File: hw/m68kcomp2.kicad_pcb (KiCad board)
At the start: 2 copper layers, 3 parts, among them U1 mc68030rc, U2 as6c8016, U3 as6c8016

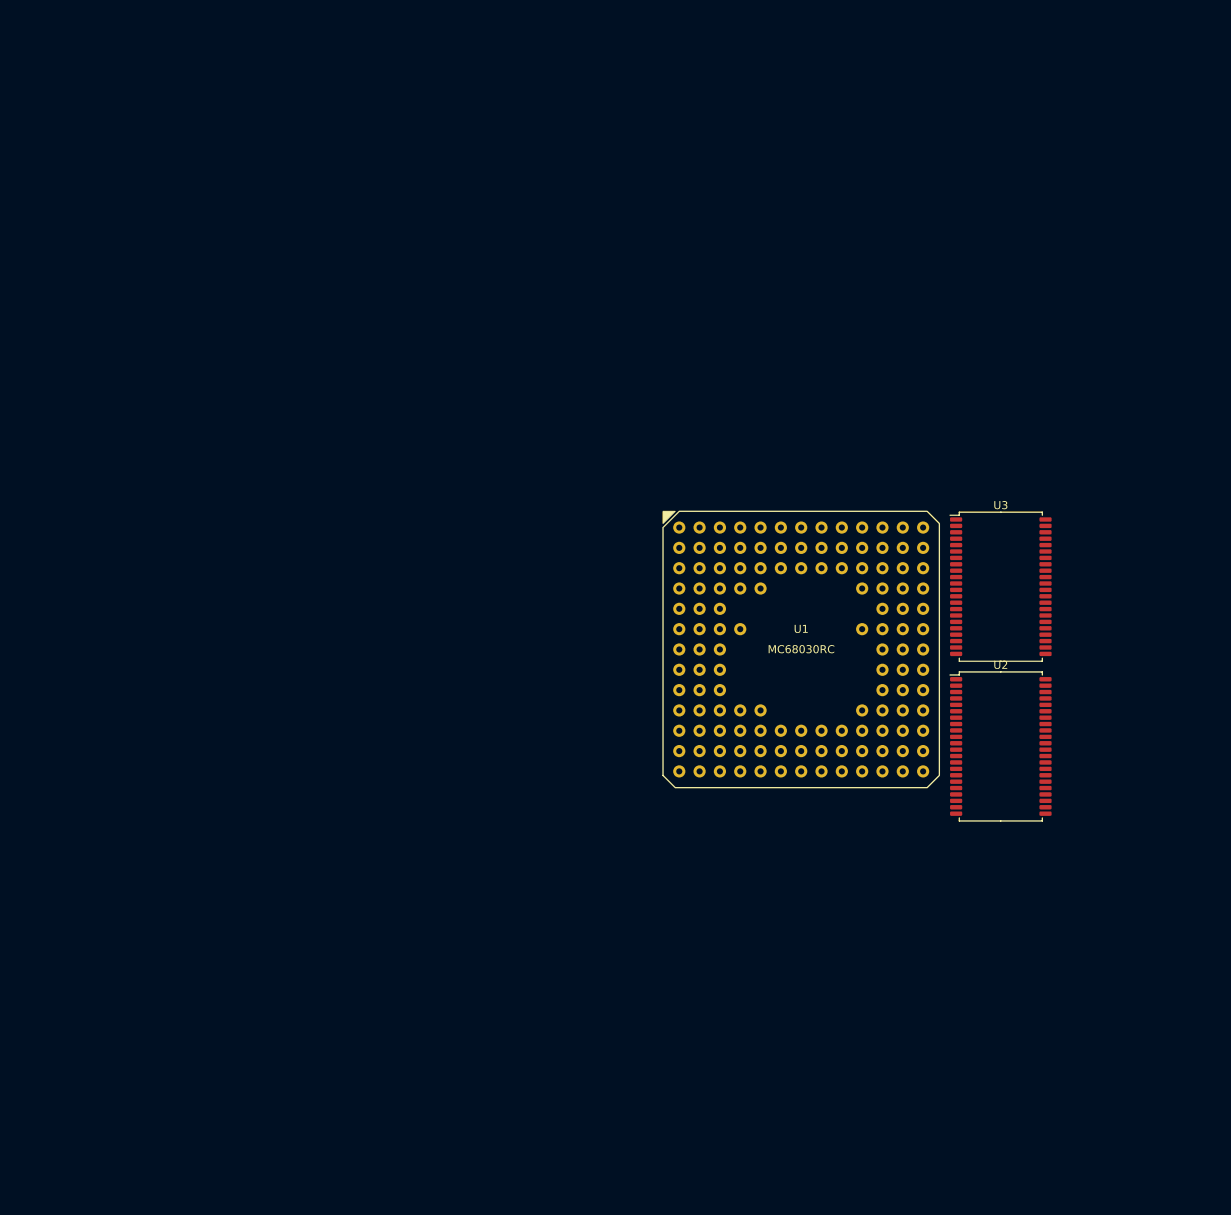
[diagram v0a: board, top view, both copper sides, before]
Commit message: BERR watchdog
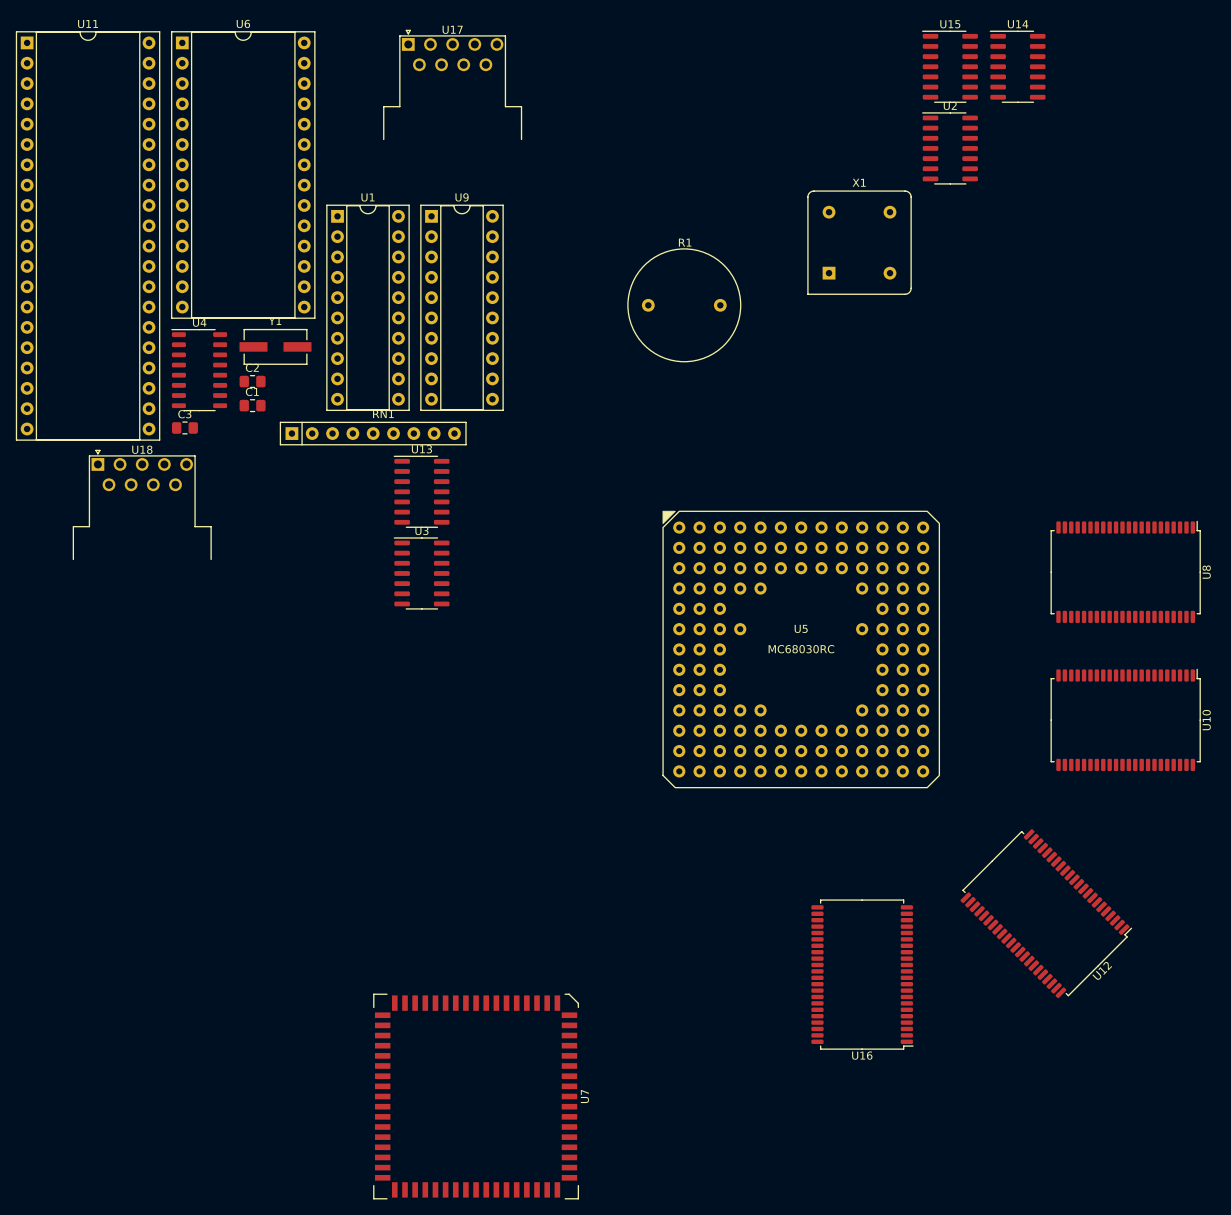
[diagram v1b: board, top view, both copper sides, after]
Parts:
- added C1: 0.1uF, Capacitor_SMD:C_0805_2012Metric_Pad1.18x1.45mm_HandSolder, F.Cu at (22.9, 43.2)
- added C2: 12pF, Capacitor_SMD:C_0805_2012Metric_Pad1.18x1.45mm_HandSolder, F.Cu at (22.9, 40.2)
- added C3: 12pF, Capacitor_SMD:C_0805_2012Metric_Pad1.18x1.45mm_HandSolder, F.Cu at (14.4, 46.0)
- added R1: 4k7, OptoDevice:R_LDR_D13.8mm_P9.0mm_Vertical, F.Cu at (72.3, 30.6)
- added RN1: 4k7, Resistor_THT:R_Array_SIP9, F.Cu at (27.8, 46.7)
- added U1: GAL16V8, Package_DIP:DIP-20_W7.62mm_Socket, F.Cu at (33.5, 19.5)
- added U10: as6c8008, Package_SO:TSOP-II-44_10.16x18.41mm_P0.8mm, F.Cu at (132.0, 82.5)
- added U11: mc68681, Package_DIP:DIP-40_W15.24mm_Socket, F.Cu at (-5.32, -2.16)
- added U12: as6c8008, Package_SO:TSOP-II-44_10.16x18.41mm_P0.8mm, F.Cu at (121.9, 106.7)
- added U13: mc1489, Package_SO:SO-14_3.9x8.65mm_P1.27mm, F.Cu at (44.0, 54.0)
- added U14: mc1488, Package_SO:SO-14_3.9x8.65mm_P1.27mm, F.Cu at (118.5, 0.82)
- added U15: mc1488, Package_SO:SO-14_3.9x8.65mm_P1.27mm, F.Cu at (110.1, 0.82)
- added U16: as6c8008, Package_SO:TSOP-II-44_10.16x18.41mm_P0.8mm, F.Cu at (99.1, 114.3)
- added U17: sera, Connector_Dsub:DSUB-9_Male_Horizontal_P2.77x2.54mm_EdgePinOffset9.40mm, F.Cu at (42.3, -1.97)
- added U18: serb, Connector_Dsub:DSUB-9_Male_Horizontal_P2.77x2.54mm_EdgePinOffset9.40mm, F.Cu at (3.53, 50.5)
- added U4: 74HC148, Package_SO:SO-16_3.9x9.9mm_P1.27mm, F.Cu at (16.2, 38.7)
- added U6: 28C256, Package_DIP:DIP-28_W15.24mm_Socket, F.Cu at (14.1, -2.16)
- added U7: mc68881, Package_LCC:PLCC-68, F.Cu at (50.8, 129.5)
- added U8: as6c8008, Package_SO:TSOP-II-44_10.16x18.41mm_P0.8mm, F.Cu at (132.0, 64.0)
- added U9: GAL16V8, Package_DIP:DIP-20_W7.62mm_Socket, F.Cu at (45.2, 19.5)
- added X1: 25.175MHz, Oscillator:Oscillator_DIP-8, F.Cu at (94.9, 26.6)
- added Y1: 3.6864MHz, Crystal:Crystal_SMD_ECS_CSM3X-2Pin_7.6x4.1mm, F.Cu at (25.7, 35.8)
- U2: value as6c8016 -> 74HC393; footprint Package_SO:TSOP-II-44_10.16x18.41mm_P0.8mm -> Package_SO:SO-14_3.9x8.65mm_P1.27mm
- U3: value as6c8016 -> 74HC10; footprint Package_SO:TSOP-II-44_10.16x18.41mm_P0.8mm -> Package_SO:SO-14_3.9x8.65mm_P1.27mm
- moved U2 75.0 mm to (110.1, 11.0)
- moved U3 72.4 mm to (44.0, 64.2)
- renumbered U1 to U5
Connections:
- U2 pad 1: /A4 -> /~{WDOG_CNT}
- U2 pad 10: /D3 -> unconnected-(U2-Pad10)
- U2 pad 11: VCC -> unconnected-(U2-Pad11)
- U2 pad 12: GND -> /WDOG_RST
- U2 pad 13: /D4 -> Net-(U2-Pad13)
- U2 pad 14: /D5 -> (no net)
- U2 pad 2: /A3 -> /WDOG_RST
- U2 pad 3: /A2 -> unconnected-(U2-Pad3)
- U2 pad 4: /A1 -> unconnected-(U2-Pad4)
- U2 pad 5: /A0 -> unconnected-(U2-Pad5)
- U2 pad 6: unconnected-(U2-Pad6) -> Net-(U2-Pad13)
- U2 pad 7: /D0 -> (no net)
- U2 pad 8: /D1 -> unconnected-(U2-Pad8)
- U2 pad 9: /D2 -> /BERR
- U3 pad 1: /A4 -> /FC2
- U3 pad 10: /D3 -> (no net)
- U3 pad 11: VCC -> (no net)
- U3 pad 12: GND -> /~{FCPU}
- U3 pad 13: /D4 -> /FC0
- U3 pad 14: /D5 -> (no net)
- U3 pad 2: /A3 -> /FC1
- U3 pad 3: /A2 -> /BERR
- U3 pad 4: /A1 -> /BERR
- U3 pad 5: /A0 -> /BERR
- U3 pad 6: unconnected-(U3-Pad6) -> /~{BERR}
- U3 pad 7: /D0 -> (no net)
- U3 pad 8: /D1 -> (no net)
- U3 pad 9: /D2 -> (no net)
- U5 pad A10: unconnected-(U1-PadA10) -> /A17
- U5 pad A11: unconnected-(U1-PadA11) -> /A15
- U5 pad A12: unconnected-(U1-PadA12) -> /A13
- U5 pad A13: unconnected-(U1-PadA13) -> /A10
- U5 pad A2: unconnected-(U1-PadA2) -> /A0
- U5 pad A3: unconnected-(U1-PadA3) -> /A30
- U5 pad A4: unconnected-(U1-PadA4) -> /A28
- U5 pad A5: unconnected-(U1-PadA5) -> /A26
- U5 pad A6: unconnected-(U1-PadA6) -> /A24
- U5 pad A7: unconnected-(U1-PadA7) -> /A23
- U5 pad A8: unconnected-(U1-PadA8) -> /A21
- U5 pad A9: unconnected-(U1-PadA9) -> /A19
- U5 pad B10: unconnected-(U1-PadB10) -> /A14
- U5 pad B11: unconnected-(U1-PadB11) -> /A12
- U5 pad B12: unconnected-(U1-PadB12) -> /A8
- U5 pad B13: unconnected-(U1-PadB13) -> /A7
- U5 pad B3: unconnected-(U1-PadB3) -> /A31
- U5 pad B4: unconnected-(U1-PadB4) -> /A29
- U5 pad B5: unconnected-(U1-PadB5) -> /A27
- U5 pad B6: unconnected-(U1-PadB6) -> /A25
- U5 pad B7: unconnected-(U1-PadB7) -> /A22
- U5 pad B8: unconnected-(U1-PadB8) -> /A20
- U5 pad B9: unconnected-(U1-PadB9) -> /A16
- U5 pad C1: unconnected-(U1-PadC1) -> /FC1
- U5 pad C10: unconnected-(U1-PadC10) -> /A11
- U5 pad C11: unconnected-(U1-PadC11) -> /A9
- U5 pad C12: unconnected-(U1-PadC12) -> /A5
- U5 pad C13: unconnected-(U1-PadC13) -> /A4
- U5 pad C4: unconnected-(U1-PadC4) -> /A1
- U5 pad C8: unconnected-(U1-PadC8) -> /A18
- U5 pad D1: unconnected-(U1-PadD1) -> /FC2
- U5 pad D11: unconnected-(U1-PadD11) -> /A6
- U5 pad D12: unconnected-(U1-PadD12) -> /A3
- U5 pad D13: unconnected-(U1-PadD13) -> /A2
- U5 pad D2: unconnected-(U1-PadD2) -> /FC0
- U5 pad E1: unconnected-(U1-PadE1) -> /CLK
- U5 pad E2: unconnected-(U1-PadE2) -> /~{AVEC}
- U5 pad G12: unconnected-(U1-PadG12) -> Net-(U4-Pad6)
- U5 pad G13: unconnected-(U1-PadG13) -> Net-(U4-Pad7)
- U5 pad H1: unconnected-(U1-PadH1) -> /~{BERR}
- U5 pad H13: unconnected-(U1-PadH13) -> Net-(U4-Pad9)
- U5 pad K11: unconnected-(U1-PadK11) -> /D5
- U5 pad K12: unconnected-(U1-PadK12) -> /D1
- U5 pad K13: unconnected-(U1-PadK13) -> /D0
- U5 pad L10: unconnected-(U1-PadL10) -> /D10
- U5 pad L11: unconnected-(U1-PadL11) -> /D7
- U5 pad L12: unconnected-(U1-PadL12) -> /D4
- U5 pad L13: unconnected-(U1-PadL13) -> /D2
- U5 pad L4: unconnected-(U1-PadL4) -> /D30
- U5 pad M10: unconnected-(U1-PadM10) -> /D12
- U5 pad M11: unconnected-(U1-PadM11) -> /D9
- U5 pad M12: unconnected-(U1-PadM12) -> /D6
- U5 pad M13: unconnected-(U1-PadM13) -> /D3
- U5 pad M3: unconnected-(U1-PadM3) -> /D29
- U5 pad M4: unconnected-(U1-PadM4) -> /D27
- U5 pad M5: unconnected-(U1-PadM5) -> /D24
- U5 pad M6: unconnected-(U1-PadM6) -> /D22
- U5 pad M7: unconnected-(U1-PadM7) -> /D20
- U5 pad M8: unconnected-(U1-PadM8) -> /D17
- U5 pad M9: unconnected-(U1-PadM9) -> /D14
- U5 pad N1: unconnected-(U1-PadN1) -> /D31
- U5 pad N10: unconnected-(U1-PadN10) -> /D15
- U5 pad N11: unconnected-(U1-PadN11) -> /D13
- U5 pad N12: unconnected-(U1-PadN12) -> /D11
- U5 pad N13: unconnected-(U1-PadN13) -> /D8
- U5 pad N2: unconnected-(U1-PadN2) -> /D28
- U5 pad N3: unconnected-(U1-PadN3) -> /D26
- U5 pad N4: unconnected-(U1-PadN4) -> /D25
- U5 pad N5: unconnected-(U1-PadN5) -> /D23
- U5 pad N6: unconnected-(U1-PadN6) -> /D21
- U5 pad N7: unconnected-(U1-PadN7) -> /D19
- U5 pad N8: unconnected-(U1-PadN8) -> /D18
- U5 pad N9: unconnected-(U1-PadN9) -> /D16

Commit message: fixed resistor footprint assignments, changed PCB to 4-layer
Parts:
- added BT1: 3V, Battery:BatteryHolder_Keystone_1060_1x2032, F.Cu at (251.5, 63.5)
- added C10: 10uF, Capacitor_SMD:C_0805_2012Metric_Pad1.18x1.45mm_HandSolder, F.Cu at (51.6, -22.9)
- added C11: 0.1u, Capacitor_SMD:C_0805_2012Metric_Pad1.18x1.45mm_HandSolder, F.Cu at (56.5, -18.2)
- added C12: 0.1uF, Capacitor_SMD:C_0805_2012Metric_Pad1.18x1.45mm_HandSolder, F.Cu at (71.1, -25.9)
- added C13: 0.1u, Capacitor_SMD:C_0805_2012Metric_Pad1.18x1.45mm_HandSolder, F.Cu at (61.5, -27.2)
- added C14: 330pF, Capacitor_SMD:C_0805_2012Metric_Pad1.18x1.45mm_HandSolder, F.Cu at (66.3, -22.9)
- added C15: 0.1u, Capacitor_SMD:C_0805_2012Metric_Pad1.18x1.45mm_HandSolder, F.Cu at (46.8, -18.8)
- added C16: 10uF, Capacitor_SMD:C_0805_2012Metric_Pad1.18x1.45mm_HandSolder, F.Cu at (42.0, -15.2)
- added C17: 0.1u, Capacitor_SMD:C_0805_2012Metric_Pad1.18x1.45mm_HandSolder, F.Cu at (66.1, -16.8)
- added C18: 0.1uF, Capacitor_SMD:C_0805_2012Metric_Pad1.18x1.45mm_HandSolder, F.Cu at (66.3, -25.9)
- added C19: 0.1u, Capacitor_SMD:C_0805_2012Metric_Pad1.18x1.45mm_HandSolder, F.Cu at (56.7, -24.2)
- added C20: 0.1u, Capacitor_SMD:C_0805_2012Metric_Pad1.18x1.45mm_HandSolder, F.Cu at (56.7, -27.2)
- added C21: 330pF, Capacitor_SMD:C_0805_2012Metric_Pad1.18x1.45mm_HandSolder, F.Cu at (76.7, -33.1)
- added C22: 0.1u, Capacitor_SMD:C_0805_2012Metric_Pad1.18x1.45mm_HandSolder, F.Cu at (46.8, -24.8)
- added C23: 0.1u, Capacitor_SMD:C_0805_2012Metric_Pad1.18x1.45mm_HandSolder, F.Cu at (66.1, -19.9)
- added C24: 0.1u, Capacitor_SMD:C_0805_2012Metric_Pad1.18x1.45mm_HandSolder, F.Cu at (56.5, -21.2)
- added C25: 0.1u, Capacitor_SMD:C_0805_2012Metric_Pad1.18x1.45mm_HandSolder, F.Cu at (61.3, -18.2)
- added C26: 0.1u, Capacitor_SMD:C_0805_2012Metric_Pad1.18x1.45mm_HandSolder, F.Cu at (51.6, -16.8)
- added C27: 0.1u, Capacitor_SMD:C_0805_2012Metric_Pad1.18x1.45mm_HandSolder, F.Cu at (51.6, -19.9)
- added C28: 0.1u, Capacitor_SMD:C_0805_2012Metric_Pad1.18x1.45mm_HandSolder, F.Cu at (71.1, -22.9)
- added C29: 0.1u, Capacitor_SMD:C_0805_2012Metric_Pad1.18x1.45mm_HandSolder, F.Cu at (61.3, -21.2)
- added C30: 0.1u, Capacitor_SMD:C_0805_2012Metric_Pad1.18x1.45mm_HandSolder, F.Cu at (46.8, -21.8)
- added C31: 0.1u, Capacitor_SMD:C_0805_2012Metric_Pad1.18x1.45mm_HandSolder, F.Cu at (81.5, -33.1)
- added C32: 0.1u, Capacitor_SMD:C_0805_2012Metric_Pad1.18x1.45mm_HandSolder, F.Cu at (42.0, -19.9)
- added C33: 0.1u, Capacitor_SMD:C_0805_2012Metric_Pad1.18x1.45mm_HandSolder, F.Cu at (61.5, -24.2)
- added C34: 0.1u, Capacitor_SMD:C_0805_2012Metric_Pad1.18x1.45mm_HandSolder, F.Cu at (46.8, -15.8)
- added C35: 0.1u, Capacitor_SMD:C_0805_2012Metric_Pad1.18x1.45mm_HandSolder, F.Cu at (51.9, -25.9)
- added C36: 0.1u, Capacitor_SMD:C_0805_2012Metric_Pad1.18x1.45mm_HandSolder, F.Cu at (76.7, -30.1)
- added C4: 12pF, Capacitor_SMD:C_0805_2012Metric_Pad1.18x1.45mm_HandSolder, F.Cu at (-103.2, 1.02)
- added C5: 12pF, Capacitor_SMD:C_0805_2012Metric_Pad1.18x1.45mm_HandSolder, F.Cu at (-108.0, 1.02)
- added C6: 12pF, Capacitor_SMD:C_0805_2012Metric_Pad1.18x1.45mm_HandSolder, F.Cu at (-124.8, 27.9)
- added C7: 12pF, Capacitor_SMD:C_0805_2012Metric_Pad1.18x1.45mm_HandSolder, F.Cu at (-112.8, 1.02)
- added C8: 10uF, Capacitor_SMD:CP_Elec_4x4.5, F.Cu at (61.1, -31.6)
- added C9: 22uF, Capacitor_SMD:CP_Elec_4x4.5, F.Cu at (53.4, -31.6)
- added D1: 1N4148, Diode_THT:D_DO-35_SOD27_P7.62mm_Horizontal, F.Cu at (-78.2, 73.4)
- added D2: 1N4148, Diode_THT:D_DO-35_SOD27_P7.62mm_Horizontal, F.Cu at (-57.0, 63.9)
- added D3: 1N4148, Diode_THT:D_DO-35_SOD27_P7.62mm_Horizontal, F.Cu at (-67.5, 74.5)
- added D4: 1N4148, Diode_THT:D_DO-35_SOD27_P7.62mm_Horizontal, F.Cu at (-67.5, 71.0)
- added D5: 1N4148, Diode_THT:D_DO-35_SOD27_P7.62mm_Horizontal, F.Cu at (-78.2, 69.8)
- added D6: 1N4148, Diode_THT:D_DO-35_SOD27_P7.62mm_Horizontal, F.Cu at (-57.0, 67.4)
- added D7: 1N4148, Diode_THT:D_DO-35_SOD27_P7.62mm_Horizontal, F.Cu at (-113.7, -2.26)
- added D8: 1N4148, Diode_THT:D_DO-35_SOD27_P7.62mm_Horizontal, F.Cu at (-102.9, -2.26)
- added D9: ACTLED, LED_SMD:LED_0805_2012Metric_Pad1.15x1.40mm_HandSolder, F.Cu at (-98.4, 1.03)
- added J1: SWRST, Connector_PinHeader_2.54mm:PinHeader_1x02_P2.54mm_Vertical, F.Cu at (-29.1, 46.0)
- added J2: CFMASTER, Connector_PinHeader_2.54mm:PinHeader_1x02_P2.54mm_Vertical, F.Cu at (-40.1, 10.1)
- added J3: AVR-ISP, Connector_IDC:IDC-Header_2x03_P2.54mm_Vertical, F.Cu at (231.1, 106.7)
- added J4: ACTLED, Connector_PinHeader_2.54mm:PinHeader_1x02_P2.54mm_Vertical, F.Cu at (-38.1, -20.3)
- added J5: ATX-24, Connector_Molex:Molex_Mini-Fit_Jr_5566-24A_2x12_P4.20mm_Vertical, F.Cu at (287.0, 121.9)
- added J6: VREG_3V3, Connector_PinHeader_2.54mm:PinHeader_1x02_P2.54mm_Vertical, F.Cu at (72.0, -32.2)
- added JP1: I/O nocache, Jumper:SolderJumper-2_P1.3mm_Bridged_RoundedPad1.0x1.5mm, F.Cu at (-44.6, 63.8)
- added R2: 10k, Resistor_SMD:R_0805_2012Metric_Pad1.20x1.40mm_HandSolder, F.Cu at (-39.6, 60.5)
- added R3: 4k7, Resistor_SMD:R_0805_2012Metric_Pad1.20x1.40mm_HandSolder, F.Cu at (-93.4, 43.2)
- added R4: 4k7, Resistor_SMD:R_0805_2012Metric_Pad1.20x1.40mm_HandSolder, F.Cu at (-113.7, 53.3)
- added R5: 4k7, Resistor_SMD:R_0805_2012Metric_Pad1.20x1.40mm_HandSolder, F.Cu at (-64.7, -3.90)
- added R6: 1k, Resistor_SMD:R_0805_2012Metric_Pad1.20x1.40mm_HandSolder, F.Cu at (-72.2, 23.2)
- added R7: 1k, Resistor_SMD:R_0805_2012Metric_Pad1.20x1.40mm_HandSolder, F.Cu at (-39.3, 0.13)
- added RN2: 4k7, Resistor_THT:R_Array_SIP9, F.Cu at (-44.5, 37.2)
- added SW1: SWRST, Button_Switch_SMD:SW_SPST_EVPBF, F.Cu at (-16.9, 38.8)
- added SW2: SWPWR, Connector_PinHeader_2.54mm:PinHeader_1x02_P2.54mm_Vertical, F.Cu at (67.3, -32.2)
- added TP1: TPCLK, TestPoint:TestPoint_Pad_D1.5mm, F.Cu at (-69.6, 88.3)
- added TP10: TP3V3, TestPoint:TestPoint_Pad_D1.5mm, F.Cu at (41.4, -8.96)
- added TP11: TPN12V, TestPoint:TestPoint_Pad_D1.5mm, F.Cu at (95.0, -45.9)
- added TP12: TP5V, TestPoint:TestPoint_Pad_D1.5mm, F.Cu at (46.2, -12.5)
- added TP2: TPRST, TestPoint:TestPoint_Pad_D1.5mm, F.Cu at (-93.5, 83.9)
- added TP3: TPRW, TestPoint:TestPoint_Pad_D1.5mm, F.Cu at (-56.5, 77.4)
- added TP4: TPAS, TestPoint:TestPoint_Pad_D1.5mm, F.Cu at (-61.1, 81.6)
- added TP5: TPSZ0, TestPoint:TestPoint_Pad_D1.5mm, F.Cu at (-46.0, 67.3)
- added TP6: TPSZ1, TestPoint:TestPoint_Pad_D1.5mm, F.Cu at (-61.1, 78.1)
- added TP7: TPDS0, TestPoint:TestPoint_Pad_D1.5mm, F.Cu at (-78.0, 98.5)
- added TP8: TPDS1, TestPoint:TestPoint_Pad_D1.5mm, F.Cu at (-25.0, 45.5)
- added TP9: TP12V, TestPoint:TestPoint_Pad_D1.5mm, F.Cu at (51.0, -13.6)
- added U19: 74LVC125, Package_SO:SO-14_3.9x8.65mm_P1.27mm, F.Cu at (256.5, 132.1)
- added U20: mc1489, Package_SO:SO-14_3.9x8.65mm_P1.27mm, F.Cu at (200.7, 55.9)
- added U21: mc1488, Package_SO:SO-14_3.9x8.65mm_P1.27mm, F.Cu at (180.3, 58.4)
- added U22: mc1488, Package_SO:SO-14_3.9x8.65mm_P1.27mm, F.Cu at (165.1, 55.9)
- added U23: sdcard, Connector_Card:SD_TE_2041021, F.Cu at (246.4, 167.6)
- added U24: sera, Connector_Dsub:DSUB-9_Male_Horizontal_P2.77x2.84mm_EdgePinOffset7.70mm_Housed_MountingHolesOffset9.12mm, F.Cu at (170.2, 40.6)
- added U25: serb, Connector_Dsub:DSUB-9_Male_Horizontal_P2.77x2.84mm_EdgePinOffset7.70mm_Housed_MountingHolesOffset9.12mm, F.Cu at (205.7, 40.6)
- added U26: 28C256, Package_DIP:DIP-28_W15.24mm_Socket, F.Cu at (144.8, 148.6)
- added U27: as6c8008, Package_SO:TSOP-II-44_10.16x18.41mm_P0.8mm, F.Cu at (205.2, 180.4)
- added U28: as6c8008, Package_SO:TSOP-II-44_10.16x18.41mm_P0.8mm, F.Cu at (205.7, 151.7)
- added U29: as6c8008, Package_SO:TSOP-II-44_10.16x18.41mm_P0.8mm, F.Cu at (181.3, 180.3)
- added U30: as6c8008, Package_SO:TSOP-II-44_10.16x18.41mm_P0.8mm, F.Cu at (181.3, 151.7)
- added U31: exp_conn, m68kcomp2:pcix8slot, F.Cu at (61.0, 70.3)
- added U32: exp_conn, m68kcomp2:pcix8slot, F.Cu at (87.1, 71.3)
- added U33: LM1117-3.3, Package_TO_SOT_SMD:SOT-223-3_TabPin2, F.Cu at (274.3, 142.2)
- added Y2: 32.768kHz, Crystal:Crystal_SMD_ECS_CSM3X-2Pin_7.6x4.1mm, F.Cu at (-54.8, 16.7)
- C1: value 0.1uF -> 10uF
- C2: value 12pF -> 10uF
- C3: value 12pF -> 0.1uF
- R1: value 4k7 -> 10k; footprint OptoDevice:R_LDR_D13.8mm_P9.0mm_Vertical -> Resistor_SMD:R_0805_2012Metric_Pad1.20x1.40mm_HandSolder
- U1: value GAL16V8 -> GAL20V8; footprint Package_DIP:DIP-20_W7.62mm_Socket -> Package_DIP:DIP-24_W7.62mm_Socket
- U10: value as6c8008 -> mc68881; footprint Package_SO:TSOP-II-44_10.16x18.41mm_P0.8mm -> Package_LCC:PLCC-68_THT-Socket
- U11: value mc68681 -> 74HC393; footprint Package_DIP:DIP-40_W15.24mm_Socket -> Package_SO:SO-14_3.9x8.65mm_P1.27mm
- U12: value as6c8008 -> ATmega328PB-A; footprint Package_SO:TSOP-II-44_10.16x18.41mm_P0.8mm -> Package_QFP:TQFP-32_7x7mm_P0.8mm
- U13: value mc1489 -> cfconn; footprint Package_SO:SO-14_3.9x8.65mm_P1.27mm -> Connector_Card:CF-Card_3M_N7E50-7516PK-20-WF
- U14: value mc1488 -> ATA0; footprint Package_SO:SO-14_3.9x8.65mm_P1.27mm -> Connector_IDC:IDC-Header_2x20_P2.54mm_Vertical
- U15: value mc1488 -> mouse; footprint Package_SO:SO-14_3.9x8.65mm_P1.27mm -> m68kcomp2:minidin6
- U16: value as6c8008 -> kbd; footprint Package_SO:TSOP-II-44_10.16x18.41mm_P0.8mm -> m68kcomp2:minidin6
- U17: value sera -> ds1501; footprint Connector_Dsub:DSUB-9_Male_Horizontal_P2.77x2.54mm_EdgePinOffset9.40mm -> Package_SO:SOIC-28W_7.5x17.9mm_P1.27mm
- U18: value serb -> mc68681; footprint Connector_Dsub:DSUB-9_Male_Horizontal_P2.77x2.54mm_EdgePinOffset9.40mm -> Package_DIP:DIP-40_W15.24mm_Socket
- U2: value 74HC393 -> GAL16V8; footprint Package_SO:SO-14_3.9x8.65mm_P1.27mm -> Package_DIP:DIP-20_W7.62mm_Socket
- U3: value 74HC10 -> NE555D; footprint Package_SO:SO-14_3.9x8.65mm_P1.27mm -> Package_SO:SOIC-8_3.9x4.9mm_P1.27mm
- U4: value 74HC148 -> 74HC10; footprint Package_SO:SO-16_3.9x9.9mm_P1.27mm -> Package_SO:SO-14_3.9x8.65mm_P1.27mm
- U5: value mc68030rc -> 74LS14; footprint m68kcomp2:mc68030rc -> Package_SO:SO-14_3.9x8.65mm_P1.27mm
- U6: value 28C256 -> 74HC148; footprint Package_DIP:DIP-28_W15.24mm_Socket -> Package_SO:SO-16_3.9x9.9mm_P1.27mm
- U7: value mc68881 -> 74HC138; footprint Package_LCC:PLCC-68 -> Package_SO:SO-16_3.9x9.9mm_P1.27mm
- U8: value as6c8008 -> mc68030rc; footprint Package_SO:TSOP-II-44_10.16x18.41mm_P0.8mm -> m68kcomp2:mc68030rc
- moved U17 229.0 mm to (251.5, 91.4)
- moved X1 218.7 mm to (-112.2, 96.9)
- moved U16 179.9 mm to (254.0, 22.9)
- moved U9 178.5 mm to (-125.2, 72.8)
- moved U14 170.1 mm to (22.1, 141.0)
- moved U2 168.6 mm to (-56.5, 37.1)
- moved U5 167.2 mm to (-75.6, 81.4)
- moved U1 133.0 mm to (-89.5, 70.2)
- moved U6 132.2 mm to (-95.9, 71.1)
- moved C2 130.8 mm to (-94.0, 99.0)
- moved C1 127.2 mm to (-97.7, 83.6)
- moved U15 125.5 mm to (233.7, 22.9), turned to 180 degrees
- moved C3 125.0 mm to (-98.8, 99.0)
- moved R1 120.5 mm to (-44.4, 60.5)
- moved U18 113.6 mm to (114.3, 25.4)
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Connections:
- C1 pad 1: VCC -> Net-(C1-Pad1)
- C3 pad 1: unconnected-(C3-Pad1) -> VCC
- C3 pad 2: unconnected-(C3-Pad2) -> GND
- R1 pad 2: /~{FPU} -> Net-(C1-Pad1)
- RN1 pad 2: /~{IRQ0} -> ~{IRQ0}
- RN1 pad 3: /~{IRQ1} -> ~{IRQ1}
- RN1 pad 4: /~{IRQ2} -> ~{IRQ2}
- RN1 pad 5: /~{IRQ3} -> ~{IRQ3}
- RN1 pad 6: /~{IRQ4} -> ~{IRQ4}
- RN1 pad 7: /~{IRQ5} -> ~{IRQ5}
- U1 pad 1: /CLK -> A13
- U1 pad 10: GND -> A22
- U1 pad 11: unconnected-(U1-Pad11) -> A23
- U1 pad 12: unconnected-(U1-Pad12) -> GND
- U1 pad 13: unconnected-(U1-Pad13) -> A24
- U1 pad 14: /WDOG_RST -> A25
- U1 pad 15: /~{WDOG_CNT} -> unconnected-(U1-Pad15)
- U1 pad 17: unconnected-(U1-Pad17) -> ~{DUARTEN}
- U1 pad 18: unconnected-(U1-Pad18) -> ~{RTCEN}
- U1 pad 19: unconnected-(U1-Pad19) -> ~{AUXEN}
- U1 pad 2: /~{AS} -> A14
- U1 pad 20: VCC -> ~{ATA1EN}
- U1 pad 3: /~{DSACK0} -> A15
- U1 pad 4: /~{DSACK1} -> A16
- U1 pad 5: /~{AVEC} -> A17
- U1 pad 6: unconnected-(U1-Pad6) -> A18
- U1 pad 7: unconnected-(U1-Pad7) -> A19
- U1 pad 8: unconnected-(U1-Pad8) -> A20
- U1 pad 9: unconnected-(U1-Pad9) -> A21
- U10 pad 1: /A4 -> D2
- U10 pad 10: /D9 -> VCC
- U10 pad 11: VCC -> /FPUCLK
- U10 pad 13: /D10 -> ~{RESET}
- U10 pad 14: /D11 -> GND
- U10 pad 16: unconnected-(U10-Pad16) -> VCC
- U10 pad 17: unconnected-(U10-Pad17) -> VCC
- U10 pad 18: /A19 -> VCC
- U10 pad 19: /A18 -> GND
- U10 pad 2: /A3 -> D1
- U10 pad 20: /A17 -> /~{DS}
- U10 pad 21: /A16 -> ~{AS}
- U10 pad 22: /A15 -> A4
- U10 pad 23: /A14 -> A3
- U10 pad 24: /A13 -> A2
- U10 pad 25: /A12 -> A1
- U10 pad 26: /A11 -> VCC
- U10 pad 27: /A10 -> VCC
- U10 pad 28: /A9 -> R/~{W}
- U10 pad 29: unconnected-(U10-Pad29) -> /~{FPUEN}
- U10 pad 3: /A2 -> D0
- U10 pad 30: unconnected-(U10-Pad30) -> GND
- U10 pad 31: /D12 -> ~{DSACK0}
- U10 pad 32: /D13 -> ~{DSACK1}
- U10 pad 33: VCC -> D31
- U10 pad 34: GND -> D30
- U10 pad 35: /D14 -> D29
- U10 pad 36: /D15 -> D28
- U10 pad 37: unconnected-(U10-Pad37) -> D27
- U10 pad 38: unconnected-(U10-Pad38) -> D26
- U10 pad 39: /A8 -> D25
- U10 pad 4: /A1 -> /~{FPU}
- U10 pad 40: unconnected-(U10-Pad40) -> D24
- U10 pad 41: unconnected-(U10-Pad41) -> GND
- U10 pad 42: /A7 -> D23
- U10 pad 43: /A6 -> VCC
- U10 pad 44: /A5 -> D22
- U10 pad 5: /A0 -> GND
- U10 pad 6: unconnected-(U10-Pad6) -> GND
- U10 pad 7: unconnected-(U10-Pad7) -> GND
- U10 pad 8: unconnected-(U10-Pad8) -> GND
- U10 pad 9: /D8 -> GND
- U11 pad 1: /A2 -> /~{WDOG_CNT}
- U11 pad 10: /RXDB -> unconnected-(U11-Pad10)
- U11 pad 11: /TXDB -> unconnected-(U11-Pad11)
- U11 pad 12: /RTRB -> /WDOG_RST
- U11 pad 13: unconnected-(U11-Pad13) -> Net-(U11-Pad13)
- U11 pad 14: /DTRB -> (no net)
- U11 pad 2: GND -> /WDOG_RST
- U11 pad 3: /A3 -> unconnected-(U11-Pad3)
- U11 pad 4: /CTSB -> unconnected-(U11-Pad4)
- U11 pad 5: /A4 -> unconnected-(U11-Pad5)
- U11 pad 6: /A5 -> Net-(U11-Pad13)
- U11 pad 7: /CTSA -> (no net)
- U11 pad 8: unconnected-(U11-Pad8) -> Net-(U11-Pad8)
- U12 pad 1: /A4 -> /io/MCLK
- U12 pad 10: /D17 -> D30
- U12 pad 11: VCC -> D31
- U12 pad 12: GND -> ~{IRQ2}
- U12 pad 13: /D18 -> /io/~{SDBUFEN}
- U12 pad 14: /D19 -> /io/~{SD_CS}
- U12 pad 15: unconnected-(U12-Pad15) -> /io/MOSI
- U12 pad 16: unconnected-(U12-Pad16) -> /io/MISO
- U12 pad 17: unconnected-(U12-Pad17) -> /io/SCK
- U12 pad 18: /A19 -> VCC
- U12 pad 19: /A18 -> A4
- U12 pad 2: /A3 -> D28
- U12 pad 20: /A17 -> unconnected-(U12-Pad20)
- U12 pad 21: /A16 -> GND
- U12 pad 22: /A15 -> A5
- U12 pad 23: /A14 -> D24
- U12 pad 24: /A13 -> D25
- U12 pad 25: /A12 -> D26
- U12 pad 26: /A11 -> D27
- U12 pad 27: /A10 -> R/~{W}
- U12 pad 28: /A9 -> ~{AUXEN}
- U12 pad 29: unconnected-(U12-Pad29) -> ~{RESET}
- U12 pad 3: /A2 -> A2
- U12 pad 30: unconnected-(U12-Pad30) -> /io/KBDATA
- U12 pad 31: /D20 -> /io/MDATA
- U12 pad 32: /D21 -> /io/KBCLK
- U12 pad 4: /A1 -> VCC
- U12 pad 5: /A0 -> GND
- U12 pad 6: unconnected-(U12-Pad6) -> A3
- U12 pad 7: unconnected-(U12-Pad7) -> ~{DSACK0}
- U12 pad 8: unconnected-(U12-Pad8) -> ~{IACK2}
- U12 pad 9: /D16 -> D29
- U13 pad 1: /RXDA_232 -> GND
- U13 pad 10: /RXDB_232 -> GND
- U13 pad 11: /CTSB -> GND
- U13 pad 12: unconnected-(U13-Pad12) -> GND
- U13 pad 13: /CTSB_232 -> VCC
- U13 pad 14: VCC -> GND
- U13 pad 2: unconnected-(U13-Pad2) -> D27
- U13 pad 3: /RXDA -> D28
- U13 pad 4: /CTSA_232 -> D29
- U13 pad 5: unconnected-(U13-Pad5) -> D30
- U13 pad 6: /CTSA -> D31
- U13 pad 7: GND -> ~{ATA0EN}
- U13 pad 8: /RXDB -> GND
- U13 pad 9: unconnected-(U13-Pad9) -> GND
- U14 pad 1: -12V -> ~{RESET}
- U14 pad 10: unconnected-(U14-Pad10) -> D19
- U14 pad 11: /RTRB_232 -> D27
- U14 pad 12: /RTRB -> D20
- U14 pad 13: unconnected-(U14-Pad13) -> D26
- U14 pad 14: +12V -> D21
- U14 pad 2: /TXDA -> GND
- U14 pad 3: /TXDA_232 -> D31
- U14 pad 4: /RTRA -> D16
- U14 pad 5: /RTRA -> D30
- U14 pad 6: /RTRA_232 -> D17
- U14 pad 7: GND -> D29
- U14 pad 8: /TXDB_232 -> D18
- U14 pad 9: /TXDB -> D28
- U15 pad 1: -12V -> /io/MDATA
- U15 pad 2: /DTRA -> unconnected-(U15-Pad2)
- U15 pad 3: /DTRA_232 -> GND
- U15 pad 4: /DTRB -> VCC
- U15 pad 5: /DTRB -> /io/MCLK
- U15 pad 6: /DTRB_232 -> unconnected-(U15-Pad6)
- U16 pad 1: /A4 -> /io/KBDATA
- U16 pad 2: /A3 -> unconnected-(U16-Pad2)
- U16 pad 3: /A2 -> GND
- U16 pad 4: /A1 -> VCC
- U16 pad 5: /A0 -> /io/KBCLK
- U16 pad 7: unconnected-(U16-Pad7) -> GND
- U17 pad 1: (no net) -> unconnected-(U17-Pad1)
- U17 pad 2: (no net) -> Net-(C6-Pad1)
- U17 pad 3: (no net) -> Net-(C7-Pad1)
- U17 pad 4: (no net) -> unconnected-(U17-Pad4)
- U17 pad 5: (no net) -> unconnected-(U17-Pad5)
- U17 pad 6: (no net) -> A6
- U17 pad 7: (no net) -> A5
- U17 pad 8: (no net) -> A4
- U17 pad 9: (no net) -> A3
- U18 pad 1: (no net) -> A2
- U18 pad 2: (no net) -> GND
- U18 pad 3: (no net) -> A3
- U18 pad 4: (no net) -> /io/CTSB
- U18 pad 5: (no net) -> A4
- U18 pad 6: (no net) -> A5
- U18 pad 7: (no net) -> /io/CTSA
- U18 pad 8: (no net) -> R/~{W}
- U18 pad 9: (no net) -> ~{DSACK0}
- U2 pad 1: /~{WDOG_CNT} -> /~{FCPU}
- U2 pad 10: unconnected-(U2-Pad10) -> GND
- U2 pad 11: unconnected-(U2-Pad11) -> A29
- U2 pad 12: /WDOG_RST -> A30
- U2 pad 13: Net-(U2-Pad13) -> A31
- U2 pad 14: (no net) -> ~{IOEN}
- U2 pad 2: /WDOG_RST -> ~{AS}
- U2 pad 3: unconnected-(U2-Pad3) -> A16
- U2 pad 4: unconnected-(U2-Pad4) -> A17
- U2 pad 5: unconnected-(U2-Pad5) -> A18
- U2 pad 6: Net-(U2-Pad13) -> A19
- U2 pad 7: (no net) -> A26
- U2 pad 8: unconnected-(U2-Pad8) -> A27
- U2 pad 9: /BERR -> A28
- U3 pad 1: /FC2 -> GND
- U3 pad 2: /FC1 -> Net-(C1-Pad1)
- U3 pad 3: /BERR -> Net-(U3-Pad3)
- U3 pad 4: /BERR -> VCC
- U3 pad 5: /BERR -> unconnected-(U3-Pad5)
- U3 pad 6: /~{BERR} -> Net-(C2-Pad1)
- U3 pad 7: (no net) -> Net-(C2-Pad1)
- U3 pad 8: (no net) -> VCC
- U4 pad 1: /~{IRQ3} -> /FC2
- U4 pad 10: VCC -> R/~{W}
- U4 pad 11: /~{IRQ0} -> R/~{W}
- U4 pad 12: /~{IRQ1} -> /~{FCPU}
- U4 pad 13: /~{IRQ2} -> /FC0
- U4 pad 14: unconnected-(U4-Pad14) -> (no net)
- U4 pad 2: /~{IRQ4} -> /FC1
- U4 pad 3: /~{IRQ5} -> Net-(U11-Pad8)
- U4 pad 4: /~{NMI} -> Net-(U11-Pad8)
- U4 pad 5: GND -> Net-(U11-Pad8)
- U4 pad 6: Net-(U4-Pad6) -> Net-(D6-Pad1)
- U4 pad 7: Net-(U4-Pad7) -> (no net)
- U4 pad 8: GND -> ~{RD}
- U4 pad 9: Net-(U4-Pad9) -> R/~{W}
- U6 pad 1: /A14 -> ~{IRQ3}
- U6 pad 10: /A0 -> VCC
- U6 pad 11: /D0 -> ~{IRQ0}
- U6 pad 12: /D1 -> ~{IRQ1}
- U6 pad 13: /D2 -> ~{IRQ2}
- U6 pad 14: GND -> unconnected-(U6-Pad14)
- U6 pad 15: /D3 -> unconnected-(U6-Pad15)
- U6 pad 16: /D4 -> VCC
- U6 pad 2: /A12 -> ~{IRQ4}
- U6 pad 3: /A7 -> ~{IRQ5}
- U6 pad 4: /A6 -> /~{NMI}
- U6 pad 5: /A5 -> GND
- U6 pad 6: /A4 -> /~{IPL2}
- U6 pad 7: /A3 -> /~{IPL1}
- U6 pad 8: /A2 -> GND
- U6 pad 9: /A1 -> /~{IPL0}
- U7 pad 1: /D2 -> A1
- U7 pad 10: VCC -> ~{IACK4}
- U7 pad 11: /FPUCLK -> ~{IACK3}
- U7 pad 12: GND -> ~{IACK2}
- U7 pad 13: /~{RESET} -> ~{IACK1}
- U7 pad 14: GND -> ~{IACK0}
- U7 pad 2: /D1 -> A2
- U7 pad 3: /D0 -> A3
- U7 pad 4: /~{FPU} -> GND
- U7 pad 5: GND -> /~{IACK}
- U7 pad 6: GND -> VCC
- U7 pad 7: GND -> unconnected-(U7-Pad7)
- U7 pad 9: GND -> ~{IACK5}
- U9 pad 1: /~{FCPU} -> CLK
- U9 pad 11: /A29 -> ~{IOEN}
- U9 pad 12: /A30 -> unconnected-(U9-Pad12)
- U9 pad 13: /A31 -> unconnected-(U9-Pad13)
- U9 pad 14: /~{IOEN} -> unconnected-(U9-Pad14)
- U9 pad 15: /~{RAMEN} -> /WDOG_RST
- U9 pad 16: /~{ROMEN} -> /~{WDOG_CNT}
- U9 pad 17: /~{IACK} -> unconnected-(U9-Pad17)
- U9 pad 18: /~{FPUEN} -> unconnected-(U9-Pad18)
- U9 pad 19: /CLK -> unconnected-(U9-Pad19)
- U9 pad 2: /~{AS} -> ~{AS}
- U9 pad 3: /A16 -> ~{DSACK0}
- U9 pad 4: /A17 -> ~{DSACK1}
- U9 pad 5: /A18 -> ~{AVEC}
- U9 pad 6: /A19 -> ~{RESET}
- U9 pad 7: /A26 -> unconnected-(U9-Pad7)
- U9 pad 8: /A27 -> unconnected-(U9-Pad8)
- U9 pad 9: /A28 -> ~{IOWAIT}
- X1 pad 5: /CLK -> CLK
- Y1 pad 1: Net-(U11-Pad32) -> Net-(C4-Pad1)
- Y1 pad 2: Net-(C2-Pad1) -> Net-(C5-Pad1)
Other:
- copper layers 2 -> 4

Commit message: started laying out board
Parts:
- moved U30 344.7 mm to (-152.7, 237.0)
- moved U8 330.2 mm to (-127.0, 203.2)
- moved U28 329.6 mm to (-112.7, 237.0)
- moved U29 319.1 mm to (-132.7, 237.0)
- moved U26 315.1 mm to (-168.0, 186.7)
- moved U10 307.5 mm to (-114.2, 272.1), turned to -90 degrees
- moved U27 303.2 mm to (-92.7, 237.0)
- moved U23 67.2 mm to (294.9, 214.1)
- moved U24 5.50 mm to (173.2, 36.0)
- moved U25 5.50 mm to (208.8, 36.0)
- moved U15 2.48 mm to (233.7, 25.3)
- moved U16 2.48 mm to (254.0, 25.3)
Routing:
- net A14: track 0.00 -> 229.3 mm, vias 0 -> 5
- net A21: track 0.00 -> 221.6 mm, vias 0 -> 5
- net A12: track 0.00 -> 215.6 mm, vias 0 -> 5
- net A13: track 0.00 -> 214.5 mm, vias 0 -> 5
- net A20: track 0.00 -> 213.1 mm, vias 0 -> 5
- net A11: track 0.00 -> 198.7 mm, vias 0 -> 5
- net A19: track 0.00 -> 198.1 mm, vias 0 -> 5
- net A18: track 0.00 -> 182.5 mm, vias 0 -> 6
- net A10: track 0.00 -> 180.1 mm, vias 0 -> 4
- net A17: track 0.00 -> 172.1 mm, vias 0 -> 5
- net A7: track 0.00 -> 170.9 mm, vias 0 -> 5
- net A16: track 0.00 -> 161.2 mm, vias 0 -> 6
- net A8: track 0.00 -> 159.0 mm, vias 0 -> 5
- net A15: track 0.00 -> 158.3 mm, vias 0 -> 4
- net A5: track 0.00 -> 156.7 mm, vias 0 -> 4
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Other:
- board outline added: 248.9 x 167.6 mm
- board text added: "U30"

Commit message: pcb layout progress
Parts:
- moved U10 430.4 mm to (282.2, 104.3)
- moved U8 364.2 mm to (223.5, 104.3)
- moved U30 340.9 mm to (156.5, 93.3)
- moved U28 333.7 mm to (188.5, 93.3)
- moved U29 313.7 mm to (156.5, 115.3)
- moved U27 306.4 mm to (188.5, 115.3)
- moved U26 305.3 mm to (120.9, 87.8)
- moved U13 274.4 mm to (-188.5, 60.9)
- moved U14 274.4 mm to (-240.0, 59.6)
- moved U31 274.4 mm to (-201.2, -11.1)
- moved U32 274.4 mm to (-175.0, -10.1)
- moved U17 190.9 mm to (70.6, 30.5)
- moved U12 156.4 mm to (376.4, 78.3)
- moved BT1 154.0 mm to (100.5, 32.9)
- moved J3 80.3 mm to (310.5, 119.0)
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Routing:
- net D30: track 58.4 -> 197.0 mm, vias 1 -> 3
- net D31: track 48.8 -> 185.5 mm, vias 0 -> 3
- net A2: track 143.9 -> 278.6 mm, vias 4 -> 7
- net D24: track 72.3 -> 205.2 mm, vias 2 -> 3
- net D25: track 65.0 -> 190.6 mm, vias 2 -> 3
- net D28: track 50.4 -> 174.5 mm, vias 0 -> 3
- net D29: track 56.2 -> 179.7 mm, vias 0 -> 3
- net A3: track 152.7 -> 267.9 mm, vias 4 -> 7
- net A1: track 51.5 -> 165.9 mm, vias 0 -> 1
- net VCC: track 107.6 -> 0.00 mm, vias 9 -> 0
- net D26: track 81.0 -> 186.0 mm, vias 0 -> 3
- net R/~{W}: track 104.5 -> 0.00 mm, vias 4 -> 0
- net D27: track 72.1 -> 176.2 mm, vias 0 -> 3
- net A6: track 142.4 -> 244.4 mm, vias 4 -> 3
- net A4: track 148.7 -> 250.6 mm, vias 4 -> 7
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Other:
- board text added: "U29"
- board text added: "as6c8008"

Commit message: 32bit buses take a lot of space
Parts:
- added TP13: TPDS, TestPoint:TestPoint_Pad_D1.5mm, F.Cu at (-8.50, -2.60)
- moved U6 343.7 mm to (241.8, 135.2), turned to 180 degrees
- moved U9 132.6 mm to (4.90, 98.6)
- moved U1 77.9 mm to (-16.2, 96.4)
- moved U2 53.5 mm to (-8.70, 61.2)
- moved U19 36.2 mm to (281.5, 144.4)
- moved U10 5.50 mm to (276.7, 104.3)
- moved U18 4.00 mm to (99.4, 72.6)
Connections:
- U10 pad 20: /~{DS} -> ~{DS}
- U31 pad B4: unconnected-(U31-PadB4) -> GND
- U31 pad B45: ~{AVEC} -> ~{DS}
- U31 pad B5: GND -> ~{AVEC}
- U32 pad B4: unconnected-(U32-PadB4) -> GND
- U32 pad B45: ~{AVEC} -> ~{DS}
- U32 pad B5: GND -> ~{AVEC}
- U8 pad K2: unconnected-(U8-PadK2) -> ~{DS}
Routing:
- net D9: track 28.2 -> 199.9 mm, vias 0 -> 3
- net D0: track 63.3 -> 222.2 mm, vias 0 -> 3
- net D2: track 54.3 -> 211.5 mm, vias 0 -> 3
- net D1: track 68.0 -> 222.9 mm, vias 0 -> 3
- net D3: track 53.6 -> 204.9 mm, vias 0 -> 3
- net D16: track 42.3 -> 180.9 mm, vias 0 -> 3
- net D17: track 47.2 -> 182.8 mm, vias 0 -> 3
- net D18: track 38.6 -> 173.6 mm, vias 0 -> 3
- net D4: track 54.5 -> 189.1 mm, vias 0 -> 3
- net D6: track 55.3 -> 188.1 mm, vias 0 -> 3
- net D19: track 40.7 -> 171.6 mm, vias 0 -> 3
- net D8: track 67.4 -> 197.9 mm, vias 0 -> 3
- net D5: track 70.9 -> 201.0 mm, vias 0 -> 3
- net D7: track 62.6 -> 189.5 mm, vias 0 -> 3
- net D10: track 71.5 -> 198.0 mm, vias 0 -> 3
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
